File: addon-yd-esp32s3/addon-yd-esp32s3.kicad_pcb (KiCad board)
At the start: 2 copper layers, 35 x 108.4 mm, 37 parts, among them J1 Conn_01x22, J2 Conn_01x22, J3 Conn_01x02, J5 Conn_01x15, Q1 Q_NMOS_DGS, Q2 Q_NMOS_DGS, Q3 DMP2160U-7, U1 DW01A, U3 TP4056, U4 TLV62565DBVR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

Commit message: completando el diseño
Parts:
- removed D3: 1N5819, Diode_SMD:D_SOD-123
- added C8: 1uF, Capacitor_SMD:C_0603_1608Metric, F.Cu at (137.0, 141.7)
- added JP1: Jumper_2_Open, Jumper:SolderJumper-2_P1.3mm_Open_TrianglePad1.0x1.5mm, B.Cu at (134.9, 49.3)
- added JP2: Jumper_2_Open, Jumper:SolderJumper-2_P1.3mm_Open_TrianglePad1.0x1.5mm, F.Cu at (154.1, 150.7)
- added TP1: TestPoint, TestPoint:TestPoint_Pad_1.5x1.5mm, F.Cu at (133.0, 148.2)
- added TP2: TestPoint, TestPoint:TestPoint_Pad_1.5x1.5mm, F.Cu at (129.9, 148.2)
- moved D2 3.42 mm to (146.7, 131.6), turned to -90 degrees
- moved C4 2.84 mm to (146.6, 135.2), turned to -90 degrees
- moved D1 2.44 mm to (135.0, 131.5), turned to -90 degrees
- moved C3 2.16 mm to (136.2, 135.2)
- moved Q3 2.03 mm to (136.5, 138.2), turned to -90 degrees
- moved R6 2.02 mm to (135.5, 141.7)
- moved L1 1.20 mm to (143.2, 141.2)
- moved R9 0.36 mm to (150.8, 149.5)
- moved D5 0.26 mm to (140.9, 136.2)
- moved C5 0.10 mm to (154.5, 147.7)
- moved R10 0.07 mm to (139.0, 136.5)
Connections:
- C5 pad 1: /Power Manager/VSUP -> Net-(JP2-B)
- J1 pad 21: +3V3 -> Net-(J1-Pin_21)
- J1 pad 22: +3V3 -> Net-(J1-Pin_21)
- Q3 pad 2: Net-(D3-K) -> /Power Manager/VSUP
- Q3 pad 3: /Power Manager/VSUP -> /Power Manager/VBAT
- U4 pad 1: /Power Manager/VSUP -> Net-(JP2-B)
- U4 pad 4: /Power Manager/VSUP -> Net-(JP2-B)
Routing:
- net +3V3: track 56.9 -> 115.8 mm
- net GND: track 28.7 -> 45.2 mm, vias 11 -> 12
- net Net-(J1-Pin_21): track 0.00 -> 13.0 mm
- net Net-(JP2-B): track 0.00 -> 7.61 mm
- net /Power Manager/VSUP: track 54.0 -> 49.0 mm
- net Net-(D2-K): track 24.1 -> 19.3 mm
- net /Power Manager/VBAT: track 33.5 -> 38.1 mm
- net Net-(D1-K): track 8.70 -> 4.77 mm
- net +5V: track 53.7 -> 56.8 mm, vias 1 -> 2
- net Net-(D3-K): track 1.86 -> 0.00 mm
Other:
- board text added: "+3V3"
- board text added: "+5V"
- board text added: "-5V+"
- board text added: "GND"
- board text added: "GPIO1"
- board text added: "GPIO2"
- board text added: "GPIO39"
- board text added: "GPIO4"
- board text added: "GPIO40"
- board text added: "GPIO5"
- board text added: "GPIO8"
- board text added: "GPIO9"
- board text added: "PLACE WHAT YOU WANT HERE"
- board text added: "RXD0"
- board text added: "TXD0"

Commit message: completando diseño PCB
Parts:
- C8: footprint Capacitor_SMD:C_0603_1608Metric -> Capacitor_SMD:C_0805_2012Metric
- J3: value Conn_01x02 -> S2B-PH-K-S(LF)(SN)
- Q1, Q2: value Q_NMOS_DGS -> SI2302
- moved C8 20.5 mm to (157.4, 139.0)
- moved Q2 20.3 mm to (157.9, 142.7), turned to -90 degrees
- moved C3 20.3 mm to (156.3, 132.3)
- moved Q3 20.3 mm to (156.6, 135.3)
- moved D4 20.2 mm to (153.6, 136.2)
- moved J5 20.2 mm to (174.0, 101.8)
- moved JP2 20.2 mm to (174.2, 148.0)
- moved R5 20.2 mm to (165.3, 145.1)
- moved TP1 20.2 mm to (153.1, 145.6)
- moved B1 20.2 mm to (161.0, 99.8)
- moved C1 20.2 mm to (151.6, 139.7)
- moved C2 20.2 mm to (164.5, 142.7)
- moved C4 20.2 mm to (166.7, 132.5)
- moved C5 20.2 mm to (174.6, 145.0)
- moved C6 20.2 mm to (168.5, 140.0)
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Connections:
- Q1 pad 1: Net-(Q1-D) -> Net-(Q1-G)
- Q1 pad 2: Net-(Q1-G) -> GND
- Q1 pad 3: GND -> Net-(Q1-D)
- Q2 pad 1: Net-(Q1-D) -> Net-(Q2-G)
- Q2 pad 2: Net-(Q2-G) -> /Power Manager/GNDV
- Q2 pad 3: /Power Manager/GNDV -> Net-(Q1-D)
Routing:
- net /Power Manager/GNDV: track 93.1 -> 95.0 mm
- net Net-(Q1-G): track 3.45 -> 2.41 mm
- net Net-(Q1-D): track 4.81 -> 3.92 mm
- net GND: track 45.2 -> 46.0 mm
- net Net-(Q2-G): track 2.04 -> 2.66 mm
- net Net-(D2-K): track 19.3 -> 19.8 mm
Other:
- board text added: "0"
- board text added: "0 mm"
- board text added: "0.0000 mm / 0.0000 mm"
- board text added: "0.01 mm"
- board text added: "0.02"
- board text added: "0.035 mm"
- board text added: "0.3000 mm"
- board text added: "1"
- board text added: "1.51 mm"
- board text added: "1.6000 mm"
- board text added: "2"
- board text added: "3.3"
- board text added: "35.0000 mm x 108.3766 mm"
- board text added: "4.5"
- board text added: "B.Cu"
- board text added: "B.Mask"
- board text added: "B.Paste"
- board text added: "B.Silkscreen"
- board text added: "BOARD CHARACTERISTICS"
- board text added: "Board Thickness:"
- board text added: "Board overall dimensions:"
- board text added: "Bottom Silk Screen"
- board text added: "Bottom Solder Mask"
- board text added: "Bottom Solder Paste"
- board text added: "Castellated pads:"
- board text added: "Color"
- board text added: "Copper Finish:"
- board text added: "Copper Layer Count:"
- board text added: "Dielectric 1"
- board text added: "Direct Printing"
- board text added: "Edge card connectors:"
- board text added: "Epsilon R"
- board text added: "F.Cu"
- board text added: "F.Mask"
- board text added: "F.Paste"
- board text added: "F.Silkscreen"
- board text added: "FR4"
- board text added: "FR4 natural"
- board text added: "Green"
- board text added: "HAL SnPb"
- board text added: "Impedance Control:"
- board text added: "Layer Name"
- board text added: "Liquid Ink"
- board text added: "Loss Tangent"
- board text added: "Material"
- board text added: "Min hole diameter:"
- board text added: "Min track/spacing:"
- board text added: "No"
- board text added: "PLACE ANYTHING HERE"
- board text added: "Plated Board Edge:"
- board text added: "Thickness (mm)"
- board text added: "Top Silk Screen"
- board text added: "Top Solder Mask"
- board text added: "Top Solder Paste"
- board text added: "Type"
- board text added: "White"
- board text added: "Yes"
- board text added: "copper"
- board text added: "core"
- board text removed: "PLACE WHAT YOU WANT HERE"

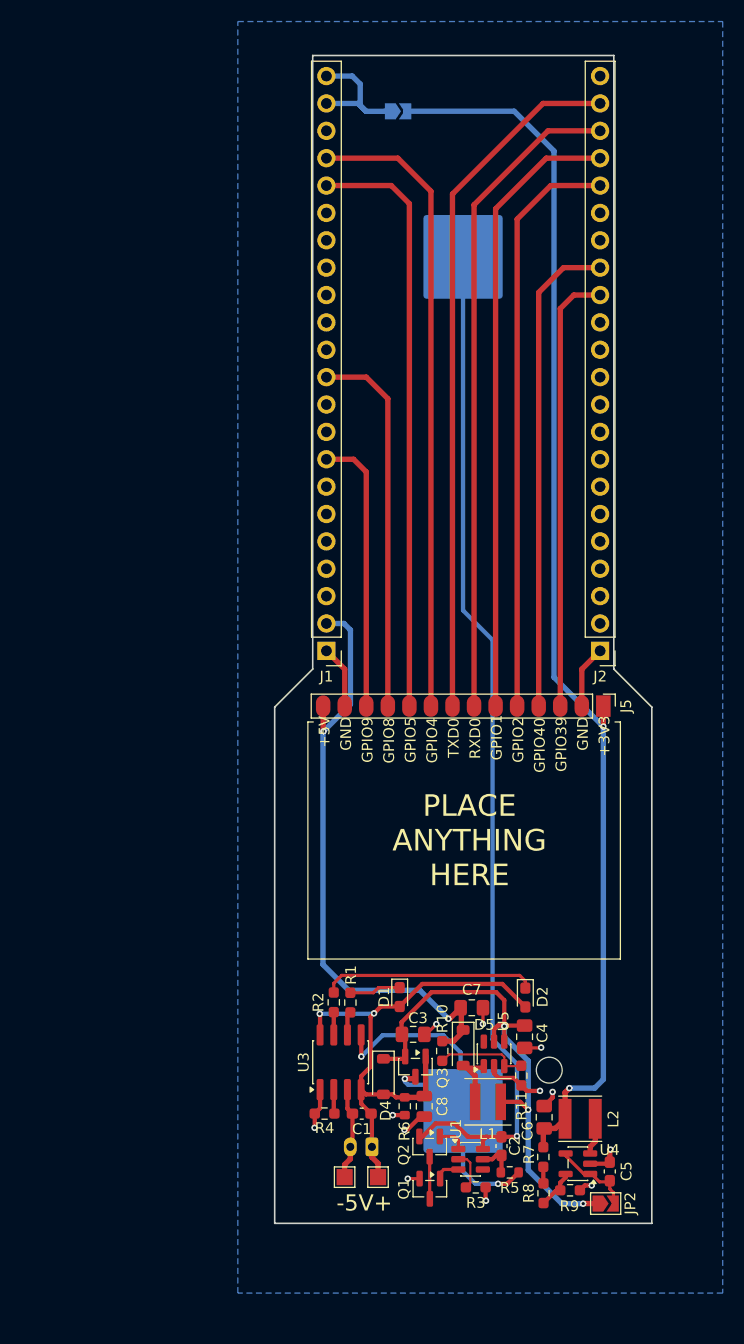
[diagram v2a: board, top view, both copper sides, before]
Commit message: cambiando el tamaño a 100 mm
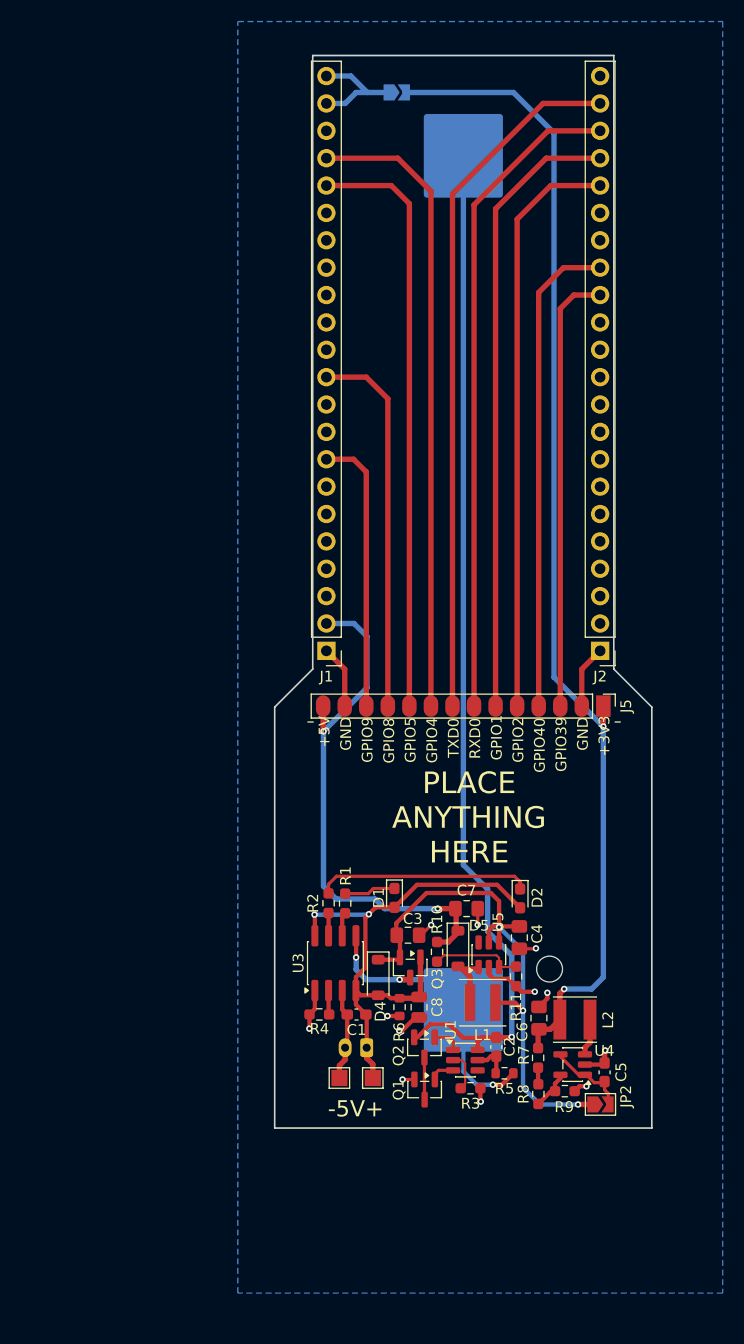
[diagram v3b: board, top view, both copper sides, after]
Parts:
- moved B1 9.38 mm to (161.0, 90.4)
- moved C8 9.21 mm to (156.9, 129.8)
- moved Q3 9.21 mm to (156.1, 126.1)
- moved R5 9.21 mm to (164.8, 135.9)
- moved TP1 9.21 mm to (152.6, 136.4)
- moved C2 9.21 mm to (164.1, 133.5)
- moved D5 9.21 mm to (160.5, 124.3)
- moved R8 9.21 mm to (168.0, 137.8)
- moved TP2 9.21 mm to (149.5, 136.4)
- moved U1 9.21 mm to (161.2, 134.7)
- moved C3 9.21 mm to (155.9, 123.1)
- moved C4 9.21 mm to (166.2, 123.3)
- moved D1 9.21 mm to (154.6, 119.6)
- moved R11 9.21 mm to (165.9, 126.9)
- moved C7 9.21 mm to (161.3, 120.6)
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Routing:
- net /Power Manager/VBAT: track 38.2 -> 27.0 mm
- net +5V: track 56.8 -> 49.2 mm
- net +3V3: track 115.8 -> 108.7 mm
- net Net-(J1-Pin_21): track 13.0 -> 10.7 mm
- net /Power Manager/GNDV: track 95.0 -> 93.8 mm
- net /Power Manager/VSUP: track 49.4 -> 50.3 mm
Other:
- board size 35 x 108.4 mm -> 35 x 99.5 mm
